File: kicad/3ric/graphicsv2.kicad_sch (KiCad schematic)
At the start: 39 parts

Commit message: update schematics
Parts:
- U? (x10): value (none) -> 74LS32
- U? (x3): value (none) -> 74LS86
- U? (x11): value (none) -> 74LS08
- U? (x3): value (none) -> 74LS04
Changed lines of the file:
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@@
     (in_bom yes) (on_board yes) (fields_autoplaced)
     (property "Reference" "U?" (id 0) (at 254 96.6302 0))
-    (property "Value" "" (id 1) (at 254 99.1671 0))
+    (property "Value" "74LS32" (id 1) (at 254 99.1671 0))
     (property "Footprint" "" (id 2) (at 254 104.14 0)
       (effects (font (size 1.27 1.27)) hide)
@@
     (in_bom yes) (on_board yes) (fields_autoplaced)
     (property "Reference" "U?" (id 0) (at 213.36 83.9302 0))
-    (property "Value" "" (id 1) (at 213.36 86.4671 0))
+    (property "Value" "74LS32" (id 1) (at 213.36 86.4671 0))
     (property "Footprint" "" (id 2) (at 213.36 91.44 0)
       (effects (font (size 1.27 1.27)) hide)
@@
     (in_bom yes) (on_board yes) (fields_autoplaced)
     (property "Reference" "U?" (id 0) (at 233.68 68.6902 0))
-    (property "Value" "" (id 1) (at 233.68 71.2271 0))
+    (property "Value" "74LS32" (id 1) (at 233.68 71.2271 0))
     (property "Footprint" "" (id 2) (at 233.68 76.2 0)
       (effects (font (size 1.27 1.27)) hide)
@@
     (in_bom yes) (on_board yes) (fields_autoplaced)
     (property "Reference" "U?" (id 0) (at 98.7552 77.5802 0))
-    (property "Value" "" (id 1) (at 98.7552 80.1171 0))
+    (property "Value" "74LS86" (id 1) (at 98.7552 80.1171 0))
     (property "Footprint" "" (id 2) (at 99.06 85.09 0)
       (effects (font (size 1.27 1.27)) hide)
@@
     (in_bom yes) (on_board yes) (fields_autoplaced)
     (property "Reference" "U?" (id 0) (at 35.56 102.9802 0))
-    (property "Value" "" (id 1) (at 35.56 105.5171 0))
+    (property "Value" "74LS08" (id 1) (at 35.56 105.5171 0))
     (property "Footprint" "" (id 2) (at 35.56 110.49 0)
       (effects (font (size 1.27 1.27)) hide)
@@
     (in_bom yes) (on_board yes) (fields_autoplaced)
     (property "Reference" "U?" (id 0) (at 78.74 114.4102 0))
-    (property "Value" "" (id 1) (at 78.74 116.9471 0))
+    (property "Value" "74LS08" (id 1) (at 78.74 116.9471 0))
     (property "Footprint" "" (id 2) (at 78.74 121.92 0)
       (effects (font (size 1.27 1.27)) hide)
@@
     (in_bom yes) (on_board yes) (fields_autoplaced)
     (property "Reference" "U?" (id 0) (at 78.74 100.4402 0))
-    (property "Value" "" (id 1) (at 78.74 102.9771 0))
+    (property "Value" "74LS08" (id 1) (at 78.74 102.9771 0))
     (property "Footprint" "" (id 2) (at 78.74 107.95 0)
       (effects (font (size 1.27 1.27)) hide)
@@
     (in_bom yes) (on_board yes) (fields_autoplaced)
     (property "Reference" "U?" (id 0) (at 254 81.3902 0))
-    (property "Value" "" (id 1) (at 254 83.9271 0))
+    (property "Value" "74LS32" (id 1) (at 254 83.9271 0))
     (property "Footprint" "" (id 2) (at 254 88.9 0)
       (effects (font (size 1.27 1.27)) hide)
@@
     (in_bom yes) (on_board yes) (fields_autoplaced)
     (property "Reference" "U?" (id 0) (at 52.07 102.9802 0))
-    (property "Value" "" (id 1) (at 52.07 105.5171 0))
+    (property "Value" "74LS04" (id 1) (at 52.07 105.5171 0))
     (property "Footprint" "" (id 2) (at 52.07 110.49 0)
       (effects (font (size 1.27 1.27)) hide)
@@
     (in_bom yes) (on_board yes) (fields_autoplaced)
     (property "Reference" "U?" (id 0) (at 148.59 91.5502 0))
-    (property "Value" "" (id 1) (at 148.59 94.0871 0))
+    (property "Value" "74LS04" (id 1) (at 148.59 94.0871 0))
     (property "Footprint" "" (id 2) (at 148.59 99.06 0)
       (effects (font (size 1.27 1.27)) hide)
@@
     (in_bom yes) (on_board yes) (fields_autoplaced)
     (property "Reference" "U?" (id 0) (at 210.82 138.5402 0))
-    (property "Value" "" (id 1) (at 210.82 141.0771 0))
+    (property "Value" "74LS32" (id 1) (at 210.82 141.0771 0))
     (property "Footprint" "" (id 2) (at 210.82 146.05 0)
       (effects (font (size 1.27 1.27)) hide)
@@
     (in_bom yes) (on_board yes) (fields_autoplaced)
     (property "Reference" "U?" (id 0) (at 133.0452 72.5002 0))
-    (property "Value" "" (id 1) (at 133.0452 75.0371 0))
+    (property "Value" "74LS86" (id 1) (at 133.0452 75.0371 0))
     (property "Footprint" "" (id 2) (at 133.35 80.01 0)
       (effects (font (size 1.27 1.27)) hide)
@@
     (in_bom yes) (on_board yes) (fields_autoplaced)
     (property "Reference" "U?" (id 0) (at 163.83 75.0402 0))
-    (property "Value" "" (id 1) (at 163.83 77.5771 0))
+    (property "Value" "74LS08" (id 1) (at 163.83 77.5771 0))
     (property "Footprint" "" (id 2) (at 163.83 82.55 0)
       (effects (font (size 1.27 1.27)) hide)
@@
     (in_bom yes) (on_board yes) (fields_autoplaced)
     (property "Reference" "U?" (id 0) (at 163.83 89.0102 0))
-    (property "Value" "" (id 1) (at 163.83 91.5471 0))
+    (property "Value" "74LS08" (id 1) (at 163.83 91.5471 0))
     (property "Footprint" "" (id 2) (at 163.83 96.52 0)
       (effects (font (size 1.27 1.27)) hide)
@@
     (in_bom yes) (on_board yes) (fields_autoplaced)
     (property "Reference" "U?" (id 0) (at 78.74 86.4702 0))
-    (property "Value" "" (id 1) (at 78.74 89.0071 0))
+    (property "Value" "74LS08" (id 1) (at 78.74 89.0071 0))
     (property "Footprint" "" (id 2) (at 78.74 93.98 0)
       (effects (font (size 1.27 1.27)) hide)
@@
     (in_bom yes) (on_board yes) (fields_autoplaced)
     (property "Reference" "U?" (id 0) (at 254 111.8702 0))
-    (property "Value" "" (id 1) (at 254 114.4071 0))
+    (property "Value" "74LS32" (id 1) (at 254 114.4071 0))
     (property "Footprint" "" (id 2) (at 254 119.38 0)
       (effects (font (size 1.27 1.27)) hide)
@@
     (in_bom yes) (on_board yes) (fields_autoplaced)
     (property "Reference" "U?" (id 0) (at 232.41 109.3302 0))
-    (property "Value" "" (id 1) (at 232.41 111.8671 0))
+    (property "Value" "74LS32" (id 1) (at 232.41 111.8671 0))
     (property "Footprint" "" (id 2) (at 232.41 116.84 0)
       (effects (font (size 1.27 1.27)) hide)
@@
     (in_bom yes) (on_board yes) (fields_autoplaced)
     (property "Reference" "U?" (id 0) (at 254 146.1602 0))
-    (property "Value" "" (id 1) (at 254 148.6971 0))
+    (property "Value" "74LS32" (id 1) (at 254 148.6971 0))
     (property "Footprint" "" (id 2) (at 254 153.67 0)
       (effects (font (size 1.27 1.27)) hide)
@@
     (in_bom yes) (on_board yes) (fields_autoplaced)
     (property "Reference" "U?" (id 0) (at 78.74 69.9602 0))
-    (property "Value" "" (id 1) (at 78.74 72.4971 0))
+    (property "Value" "74LS08" (id 1) (at 78.74 72.4971 0))
     (property "Footprint" "" (id 2) (at 78.74 77.47 0)
       (effects (font (size 1.27 1.27)) hide)
@@
     (in_bom yes) (on_board yes) (fields_autoplaced)
     (property "Reference" "U?" (id 0) (at 35.56 77.5802 0))
-    (property "Value" "" (id 1) (at 35.56 80.1171 0))
+    (property "Value" "74LS08" (id 1) (at 35.56 80.1171 0))
     (property "Footprint" "" (id 2) (at 35.56 85.09 0)
       (effects (font (size 1.27 1.27)) hide)
@@
     (in_bom yes) (on_board yes) (fields_autoplaced)
     (property "Reference" "U?" (id 0) (at 114.3 89.0102 0))
-    (property "Value" "" (id 1) (at 114.3 91.5471 0))
+    (property "Value" "74LS08" (id 1) (at 114.3 91.5471 0))
     (property "Footprint" "" (id 2) (at 114.3 96.52 0)
       (effects (font (size 1.27 1.27)) hide)
@@
     (in_bom yes) (on_board yes) (fields_autoplaced)
     (property "Reference" "U?" (id 0) (at 163.83 109.3302 0))
-    (property "Value" "" (id 1) (at 163.83 111.8671 0))
+    (property "Value" "74LS08" (id 1) (at 163.83 111.8671 0))
     (property "Footprint" "" (id 2) (at 163.83 116.84 0)
       (effects (font (size 1.27 1.27)) hide)
@@
     (in_bom yes) (on_board yes) (fields_autoplaced)
     (property "Reference" "U?" (id 0) (at 131.7752 111.8702 0))
-    (property "Value" "" (id 1) (at 131.7752 114.4071 0))
+    (property "Value" "74LS86" (id 1) (at 131.7752 114.4071 0))
     (property "Footprint" "" (id 2) (at 132.08 119.38 0)
       (effects (font (size 1.27 1.27)) hide)
@@
     (in_bom yes) (on_board yes) (fields_autoplaced)
     (property "Reference" "U?" (id 0) (at 163.83 123.3002 0))
-    (property "Value" "" (id 1) (at 163.83 125.8371 0))
+    (property "Value" "74LS08" (id 1) (at 163.83 125.8371 0))
     (property "Footprint" "" (id 2) (at 163.83 130.81 0)
       (effects (font (size 1.27 1.27)) hide)
@@
     (in_bom yes) (on_board yes) (fields_autoplaced)
     (property "Reference" "U?" (id 0) (at 232.41 94.0902 0))
-    (property "Value" "" (id 1) (at 232.41 96.6271 0))
+    (property "Value" "74LS32" (id 1) (at 232.41 96.6271 0))
     (property "Footprint" "" (id 2) (at 232.41 101.6 0)
       (effects (font (size 1.27 1.27)) hide)
@@
     (in_bom yes) (on_board yes) (fields_autoplaced)
     (property "Reference" "U?" (id 0) (at 231.14 127.1102 0))
-    (property "Value" "" (id 1) (at 231.14 129.6471 0))
+    (property "Value" "74LS32" (id 1) (at 231.14 129.6471 0))
     (property "Footprint" "" (id 2) (at 231.14 134.62 0)
       (effects (font (size 1.27 1.27)) hide)
@@
     (in_bom yes) (on_board yes) (fields_autoplaced)
     (property "Reference" "U?" (id 0) (at 52.07 77.5802 0))
-    (property "Value" "" (id 1) (at 52.07 80.1171 0))
+    (property "Value" "74LS04" (id 1) (at 52.07 80.1171 0))
     (property "Footprint" "" (id 2) (at 52.07 85.09 0)
       (effects (font (size 1.27 1.27)) hide)

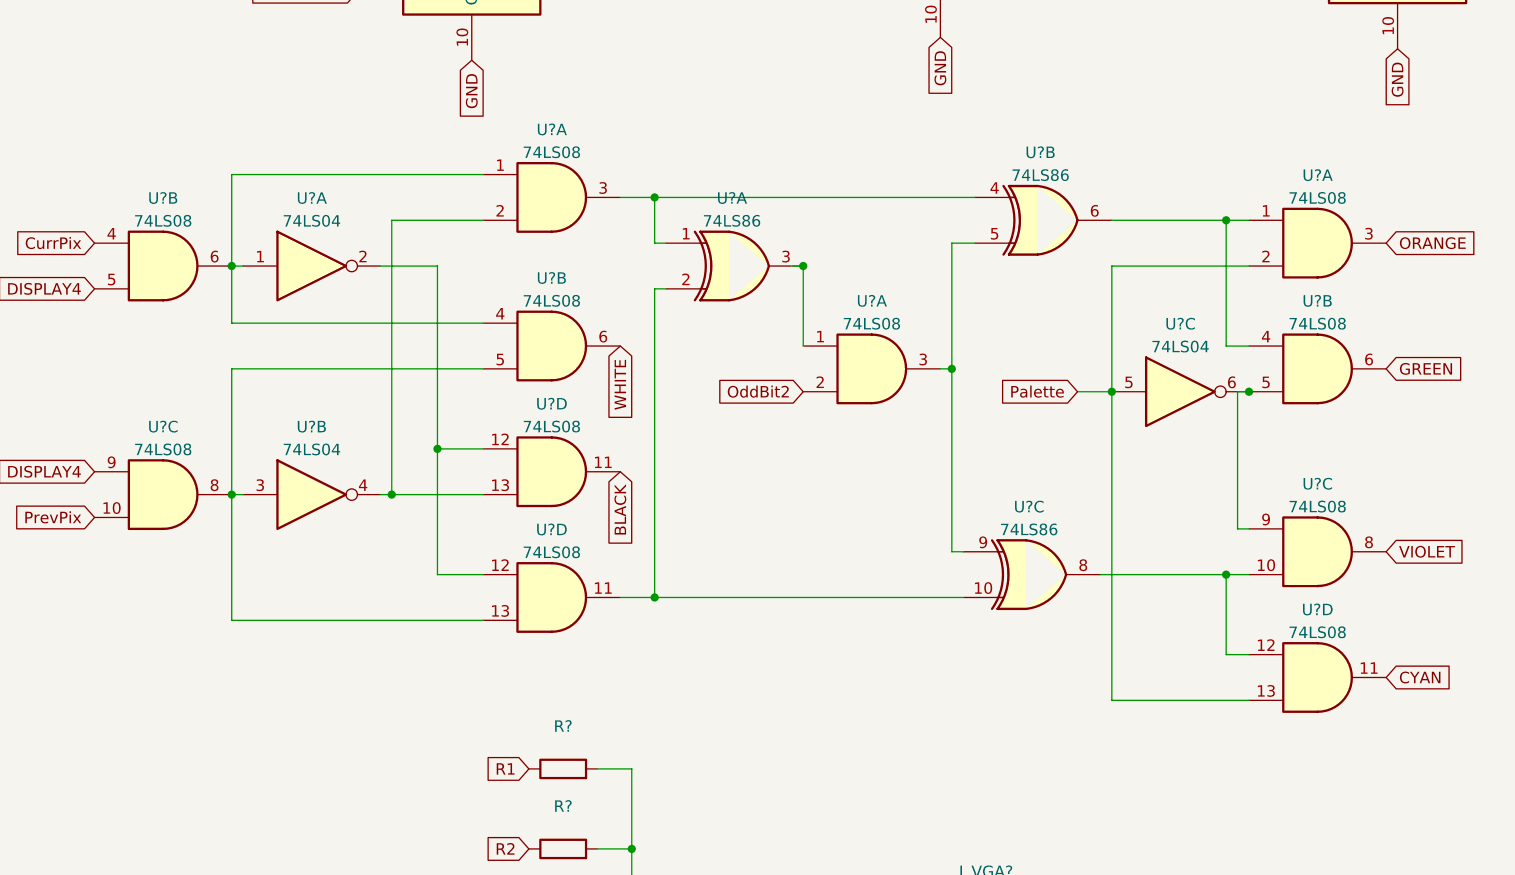
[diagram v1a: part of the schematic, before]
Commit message: upgraded to kicad 8, updates to schematic - added snes controllers, mouse port, many fixes
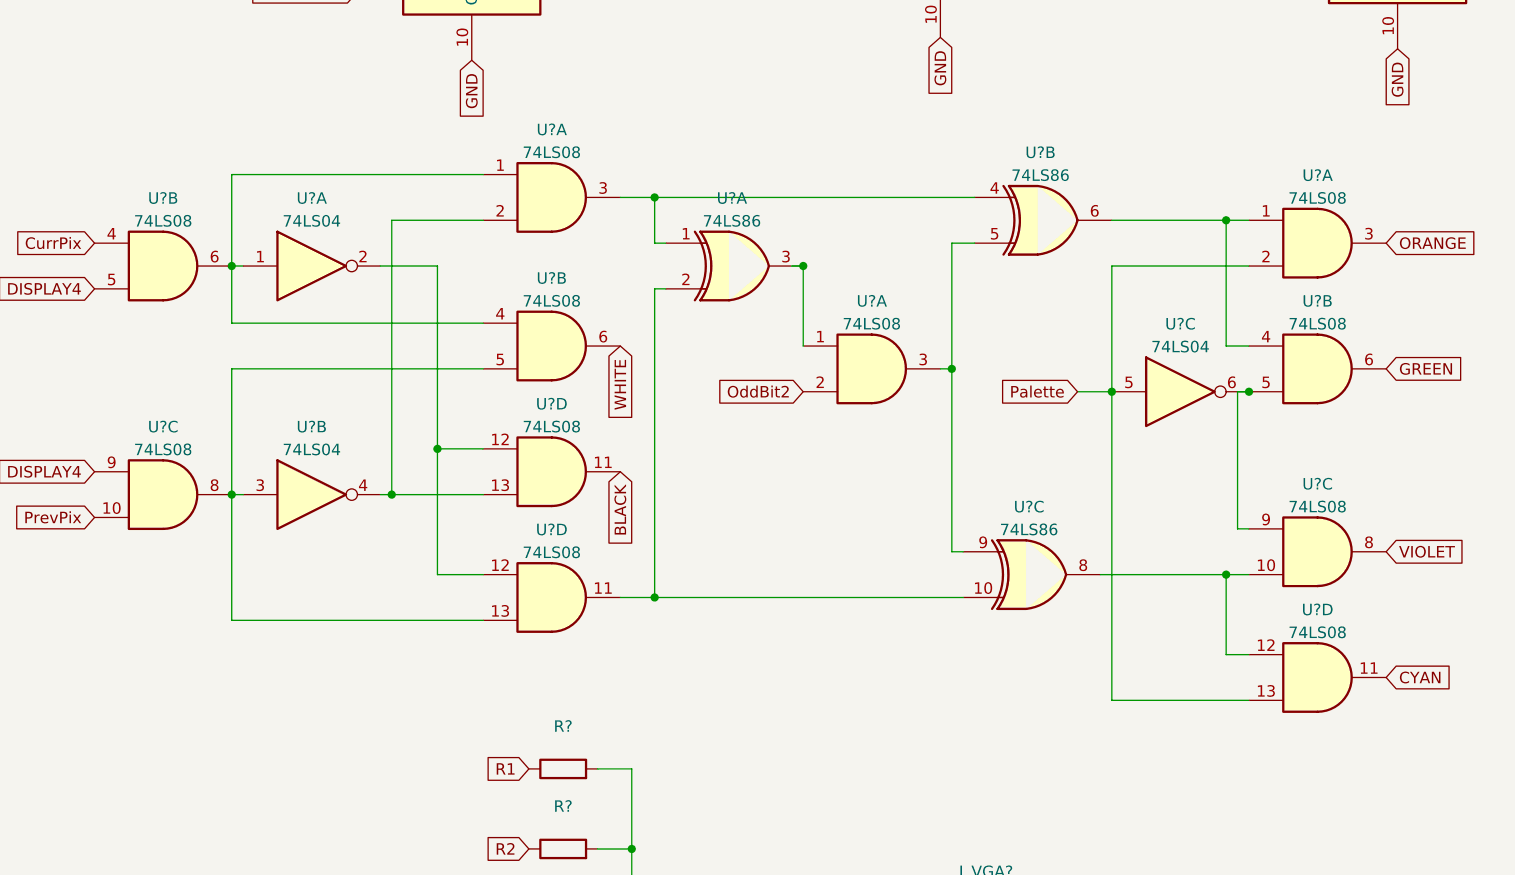
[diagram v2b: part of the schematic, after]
